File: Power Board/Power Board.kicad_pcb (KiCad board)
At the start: 2 copper layers, 55.9 x 58.4 mm, 55 parts, among them J1 Conn_02x10_Odd_Even, J2 Conn_01x02, J3 Conn_01x02, J4 Conn_01x02, J5 Conn_01x02, Q1 SI7135DP, Q2 SI7135DP, Q3 SI7135DP, Q4 SI7135DP, Q5 SI7135DP, Q6 SI7135DP, U1 LTC4417CGN, U2 TPS54308DDC, U3 LTC3130-1

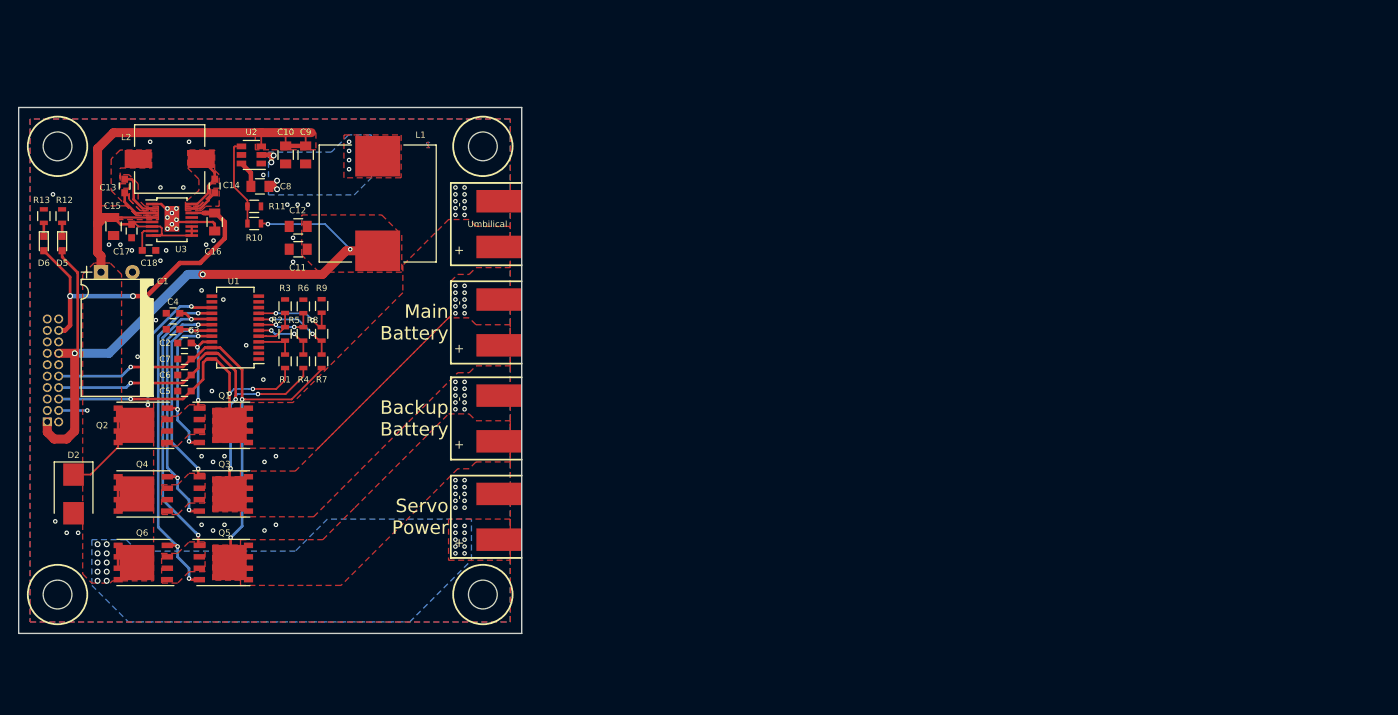
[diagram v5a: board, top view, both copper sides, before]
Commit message: Finally ready to redo power PCB
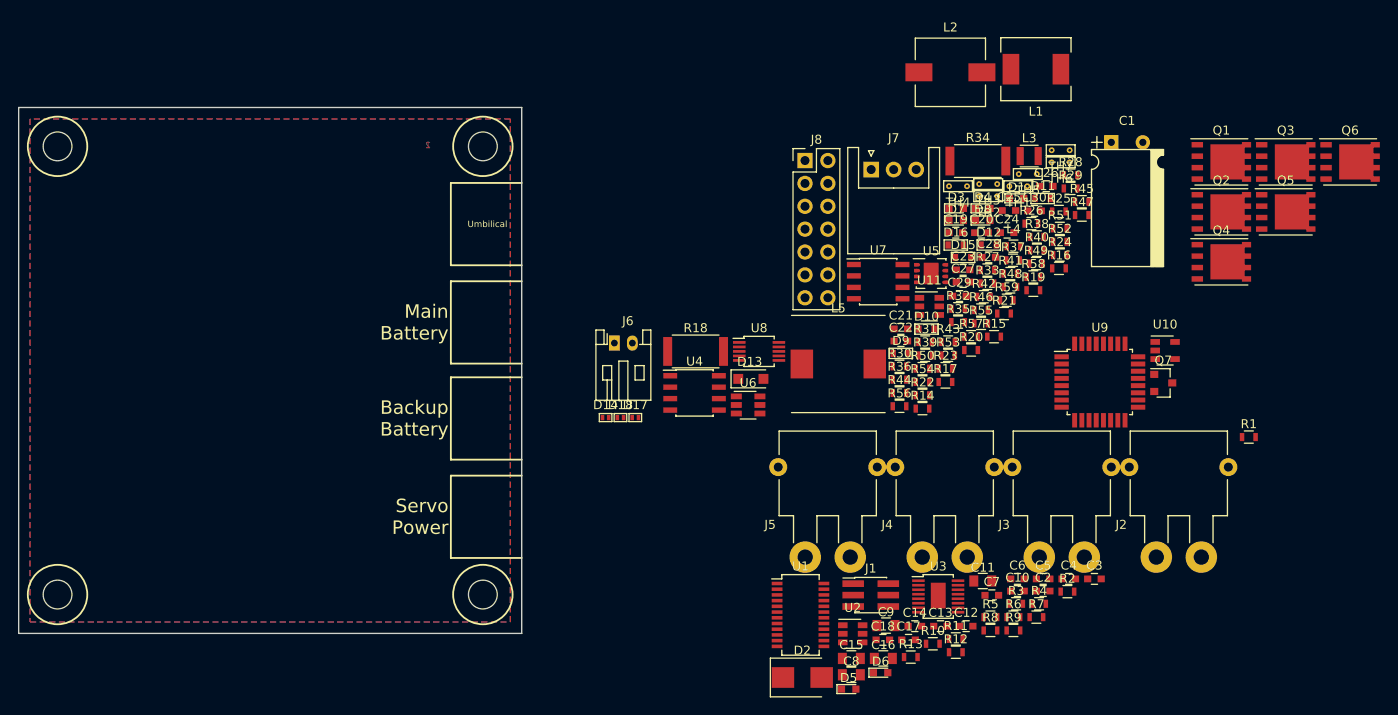
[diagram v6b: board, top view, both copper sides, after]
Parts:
- added C19: 0.1 µF, Capacitors_SMD:C_0603, F.Cu at (299.9, 97.0)
- added C20: 0.1 µF, Capacitors_SMD:C_0603, F.Cu at (302.8, 97.0)
- added C21: 0.1 µF, Capacitors_SMD:C_0603, F.Cu at (293.8, 107.7)
- added C22: 0.1 µF, Capacitors_SMD:C_0603, F.Cu at (293.8, 109.0)
- added C23: 0.33 µF, Capacitors_SMD:C_0603, F.Cu at (300.7, 101.1)
- added C24: 10 µF, Capacitors_SMD:C_0603, F.Cu at (305.6, 97.0)
- added C25: 10 µF, Capacitors_SMD:C_0603, F.Cu at (305.8, 94.5)
- added C26: 0.1 µF, Capacitors_SMD:C_0603, F.Cu at (310.0, 91.8)
- added C27: 0.1 µF, Capacitors_SMD:C_0603, F.Cu at (300.7, 102.4)
- added C28: 4.7 µF, Capacitors_SMD:C_0603, F.Cu at (303.6, 99.7)
- added C29: 270 pF, Capacitors_SMD:C_0603, F.Cu at (300.3, 104.0)
- added C30: 10 µF, Capacitors_SMD:C_0603, F.Cu at (308.7, 94.5)
- added D1: LED_B, LEDs:LED_0603, F.Cu at (306.7, 93.2)
- added D10: 12V TVS, Custom Parts:TVS_0603, F.Cu at (296.7, 107.7)
- added D11: 12V TVS, Custom Parts:TVS_0603, F.Cu at (309.6, 93.2)
- added D12: 12V TVS, Custom Parts:TVS_0603, F.Cu at (303.6, 98.3)
- added D13: D_Schottky, Diodes_SMD:D_SOD-123F, F.Cu at (277.2, 113.2)
- added D14: 3.3V TVS, Custom Parts:TVS_0402, F.Cu at (261.0, 117.5)
- added D15: 12V TVS, Custom Parts:TVS_0603, F.Cu at (300.7, 99.7)
- added D16: 12V TVS, Custom Parts:TVS_0603, F.Cu at (299.9, 98.3)
- added D17: 3.3V TVS, Custom Parts:TVS_0402, F.Cu at (264.3, 117.5)
- added D18: 3.3V TVS, Custom Parts:TVS_0402, F.Cu at (262.7, 117.5)
- added D3: LED_B, LEDs:LED_0603, F.Cu at (300.0, 94.3)
- added D4: LED_B, LEDs:LED_0603, F.Cu at (302.9, 94.3)
- added D7: LED_B, LEDs:LED_0603, F.Cu at (300.0, 95.6)
- added D8: LED_G, LEDs:LED_0603, F.Cu at (302.9, 95.6)
- added D9: 12V TVS, Custom Parts:TVS_0603, F.Cu at (293.8, 110.4)
- added HS1: Heatsink, Custom Parts:HS_ATS1099, F.Cu at (270.8, 97.7)
- added J6: Conn_01x02, Connectors_JST:JST_PH_S2B-PH-K_02x2.00mm_Angled, F.Cu at (262.0, 109.2)
- added J7: Conn_01x03, Connectors_JST:JST_XH_S03B-XH-A_03x2.50mm_Angled, F.Cu at (290.5, 90.0)
- added J8: Conn_02x07_Odd_Even, Pin_Headers:Pin_Header_Straight_2x07_Pitch2.54mm, F.Cu at (283.2, 89.0)
- added L3: 10 µH, Custom Parts:L_1008, F.Cu at (308.1, 88.5)
- added L4: 220 Ω @ 100 MHz, Inductors_SMD:L_0603, F.Cu at (306.3, 98.5)
- added L5: 10 µH, Custom Parts:L_SLF10165, F.Cu at (286.9, 111.6)
- added Q7: DMG2305UX, TO_SOT_Packages_SMD:SOT-23, F.Cu at (323.0, 113.7)
- added R14: 1 kΩ, Resistors_SMD:R_0603, F.Cu at (296.2, 116.5)
- added R15: 1 kΩ, Resistors_SMD:R_0603, F.Cu at (304.2, 108.5)
- added R16: 1 kΩ, Resistors_SMD:R_0603, F.Cu at (311.4, 100.9)
- added R17: 1 kΩ, Resistors_SMD:R_0603, F.Cu at (298.8, 113.5)
- added R18: 0.124Ω, Resistors_SMD:R_2512, F.Cu at (271.0, 110.2)
- added R19: 8.25 kΩ, Resistors_SMD:R_0603, F.Cu at (308.5, 103.4)
- added R20: 1 kΩ, Resistors_SMD:R_0603, F.Cu at (301.6, 110.0)
- added R21: 22.1 kΩ, Resistors_SMD:R_0603, F.Cu at (305.3, 105.9)
- added R22: 100 Ω, Resistors_SMD:R_0603, F.Cu at (296.2, 115.0)
- added R23: 100 kΩ, Resistors_SMD:R_0603, F.Cu at (298.8, 112.1)
- added R24: 100 kΩ, Resistors_SMD:R_0603, F.Cu at (311.5, 99.4)
- added R25: 100 kΩ, Resistors_SMD:R_0603, F.Cu at (311.4, 94.6)
- added R26: 140 kΩ, Resistors_SMD:R_0603, F.Cu at (308.3, 96.0)
- added R27: 10 Ω, Resistors_SMD:R_0603, F.Cu at (303.4, 101.1)
- added R28: 10 kΩ, Resistors_SMD:R_0603, F.Cu at (312.7, 90.6)
- added R29: 10 kΩ, Resistors_SMD:R_0603, F.Cu at (312.7, 92.0)
- added R30: 100 kΩ, Resistors_SMD:R_0603, F.Cu at (293.7, 111.8)
- added R31: 100 kΩ, Resistors_SMD:R_0603, F.Cu at (296.5, 109.1)
- added R32: 100 kΩ, Resistors_SMD:R_0603, F.Cu at (300.2, 105.4)
- added R33: 10 kΩ, Resistors_SMD:R_0603, F.Cu at (303.4, 102.6)
- added R34: 2.5 mΩ, Resistors_SMD:R_2512, F.Cu at (302.4, 89.0)
- added R35: 10 kΩ, Resistors_SMD:R_0603, F.Cu at (300.2, 106.9)
- added R36: 10 kΩ, Resistors_SMD:R_0603, F.Cu at (293.7, 113.3)
- added R37: 64.9 kΩ, Resistors_SMD:R_0603, F.Cu at (306.3, 100.0)
- added R38: 64.9 kΩ, Resistors_SMD:R_0603, F.Cu at (308.9, 97.4)
- added R39: 121 kΩ, Resistors_SMD:R_0603, F.Cu at (296.5, 110.6)
- added R40: 121 kΩ, Resistors_SMD:R_0603, F.Cu at (308.9, 98.9)
- added R41: 121 kΩ, Resistors_SMD:R_0603, F.Cu at (306.0, 101.5)
- added R42: 10 kΩ, Resistors_SMD:R_0603, F.Cu at (303.0, 104.1)
- added R43: 10 kΩ, Resistors_SMD:R_0603, F.Cu at (299.1, 109.1)
- added R44: 10 kΩ, Resistors_SMD:R_0603, F.Cu at (293.7, 114.8)
- added R45: 64.9 kΩ, Resistors_SMD:R_0603, F.Cu at (313.9, 93.5)
- added R46: 64.9 kΩ, Resistors_SMD:R_0603, F.Cu at (302.7, 105.6)
- added R47: 121 kΩ, Resistors_SMD:R_0603, F.Cu at (313.9, 95.0)
- added R48: 121 kΩ, Resistors_SMD:R_0603, F.Cu at (306.0, 103.0)
- added R49: 121 kΩ, Resistors_SMD:R_0603, F.Cu at (308.8, 100.4)
- added R50: 10 kΩ, Resistors_SMD:R_0603, F.Cu at (296.2, 112.1)
- added R51: 10 kΩ, Resistors_SMD:R_0603, F.Cu at (311.5, 96.5)
- added R52: 10 kΩ, Resistors_SMD:R_0603, F.Cu at (311.5, 98.0)
- added R53: 121 kΩ, Resistors_SMD:R_0603, F.Cu at (299.1, 110.6)
- added R54: 64.9 kΩ, Resistors_SMD:R_0603, F.Cu at (296.2, 113.5)
- added R55: 64.9 kΩ, Resistors_SMD:R_0603, F.Cu at (302.7, 107.0)
- added R56: 10 kΩ, Resistors_SMD:R_0603, F.Cu at (293.7, 116.2)
- added R57: 95.3 kΩ, Resistors_SMD:R_0603, F.Cu at (301.6, 108.5)
- added R58: 51 kΩ, Resistors_SMD:R_0603, F.Cu at (308.5, 101.9)
- added R59: 13.3 kΩ, Resistors_SMD:R_0603, F.Cu at (305.6, 104.5)
- added TH1: NXFT15XH103FA2B100, Custom Parts:Thermistor_Through_Hole_Tiny, F.Cu at (306.9, 91.8)
- added TH2: NXFT15XH103FA2B100, Custom Parts:Thermistor_Through_Hole_Tiny, F.Cu at (303.5, 92.9)
- added TH3: NXFT15XH103FA2B100, Custom Parts:Thermistor_Through_Hole_Tiny, F.Cu at (303.5, 91.6)
- added TH4: NXFT15XH103FA2B100, Custom Parts:Thermistor_Through_Hole_Tiny, F.Cu at (300.2, 91.8)
- added TH5: NXFT15XH103FA2B100, Custom Parts:Thermistor_Through_Hole_Tiny, F.Cu at (307.9, 90.5)
- added TH6: NXFT15XH103FA2B100, Custom Parts:Thermistor_Through_Hole_Tiny, F.Cu at (311.6, 89.2)
- added TH7: NXFT15XH103FA2B100, Custom Parts:Thermistor_Through_Hole_Tiny, F.Cu at (311.6, 87.8)
- added U10: LMR62014XMF, TO_SOT_Packages_SMD:SOT-23-5, F.Cu at (323.2, 110.1)
- added U11: TPS22810, TO_SOT_Packages_SMD:SOT-23-6, F.Cu at (297.0, 105.2)
- added U4: BQ2057WSNTR, Housings_SOIC:SOIC-8_3.9x4.9mm_Pitch1.27mm, F.Cu at (270.9, 114.8)
- added U5: BQ29209DRBT, Housings_SON:Texas_S-PVSON-N8, F.Cu at (297.2, 101.5)
- added U6: LT6700CS6-1, TO_SOT_Packages_SMD:TSOT-23-6, F.Cu at (276.9, 116.1)
- added U7: STS8C5H30L, Housings_SOIC:SOIC-8_3.9x4.9mm_Pitch1.27mm, F.Cu at (291.3, 102.4)
- added U8: LTC4150, Housings_SSOP:MSOP-10_3x3mm_Pitch0.5mm, F.Cu at (278.1, 110.2)
- added U9: ATxmega32E5-AU, Housings_QFP:TQFP-32_7x7mm_Pitch0.8mm, F.Cu at (315.9, 113.6)
- C1: value 470 uF -> 470 µF; footprint Custom Footprints:CP_Radial_Horiz_D8.0mm_L13.00mm_P3.50mm -> Custom Parts:CP_Radial_Horiz_D8.0mm_L13.00mm_P3.50mm
- C10: value 15 uF -> 4.7 µF; footprint Capacitors_SMD:C_0805 -> Capacitors_SMD:C_0603
- C11: value 22 uF -> 47 µF
- C12: value 22 uF -> 4.7 µF; footprint Capacitors_SMD:C_0805 -> Capacitors_SMD:C_0603
- C15: value 15 uF -> 15 µF
- C16: value 22 uF -> 22 µF
- C17: value 1 uF -> 1 µF
- C18: value 4.7 uF -> 4.7 µF
- C2, C3, C4, C5, C6, C7, C8: value 0.1 uF -> 0.1 µF
- C9: value 15 uF -> 22 µF
- J1: value Conn_02x10_Odd_Even -> Conn_02x03_Odd_Even; footprint Pin_Headers:Pin_Header_Straight_2x10_Pitch1.27mm -> Pin_Headers:Pin_Header_Straight_2x03_Pitch1.27mm_SMD; moved to F.Cu
- J2, J3, J4, J5: footprint Custom Footprints:High_Current_Wires -> Custom Parts:XT30_Angled
- L1: value 18 uH -> 2.2 µH; footprint Inductors_SMD:L_Wuerth_HCI-1365 -> Custom Parts:L_SRP6540
- L2: value 15 uH -> 15 µH; footprint Custom Footprints:L_Wuerth_7447779115 -> Custom Parts:L_Wuerth_7447779115
- Q1, Q2, Q3, Q4, Q5, Q6: value SI7135DP -> SI7157DP; footprint Custom Footprints:PowerPAK_SO-8 -> Custom Parts:PowerPAK_SO-8
- R10: value 100 kΩ -> 33.2 kΩ
- R11: value 22 kΩ -> 10 kΩ
- U2: value TPS54308DDC -> TPS564208DDCT
- moved Q6 141.2 mm to (343.7, 89.1), turned to 0 degrees
- moved Q5 124.3 mm to (336.6, 94.7)
- moved Q3 123.6 mm to (336.6, 89.1)
- moved Q4 122.5 mm to (329.4, 100.2), turned to 0 degrees
- moved Q2 122.1 mm to (329.4, 94.7), turned to 0 degrees
- moved Q1 114.7 mm to (329.4, 89.1)
- moved C1 113.1 mm to (317.2, 86.9)
- moved R12 110.5 mm to (299.9, 143.6), turned to 0 degrees
- moved R13 108.0 mm to (294.9, 144.1), turned to 0 degrees
- moved R1 107.4 mm to (332.5, 119.7), turned to 0 degrees
- moved C3 106.0 mm to (315.3, 135.4), turned to 0 degrees
- moved D6 104.5 mm to (291.6, 145.8), turned to 0 degrees
- moved C4 103.8 mm to (312.5, 135.4), turned to 0 degrees
- moved C13 103.0 mm to (298.2, 140.7), turned to 0 degrees
- moved D5 100.4 mm to (288.0, 147.7), turned to 0 degrees
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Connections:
- C10 pad 1: /VCC_IN -> GND
- C10 pad 2: GND -> /BAT_CELL_2
- C12 pad 1: +3V3 -> Net-(C12-Pad1)
- C12 pad 2: GND -> Net-(C12-Pad2)
- C6 pad 2: /BAT_VCC -> /BAT_CELL_2
- J1 pad 1: +3V3 -> Net-(J1-Pad1)
- J1 pad 2: GND -> +3V3
- J1 pad 4: /VCC_IN -> (no net)
- J1 pad 5: (no net) -> Net-(J1-Pad5)
- J1 pad 6: /UMB_VCC -> GND
- J4 pad 1: /BAT_VCC -> /BAT_CELL_2_CONN
- Q3 pad 1: /BAT_VCC -> /BAT_CELL_2
- R4 pad 2: /BAT_VCC -> /BAT_CELL_2
- U1 pad 10: (no net) -> /SEL_~VALID1~
- U1 pad 11: (no net) -> /SEL_~VALID2~
- U1 pad 12: (no net) -> /SEL_~VALID3~
- U1 pad 2: (no net) -> /SEL_~SHDN~
- U1 pad 23: /BAT_VCC -> /BAT_CELL_2
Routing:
- net /VCC_IN: track 106.1 -> 0.00 mm, vias 23 -> 0
- net +3V3: track 80.1 -> 0.00 mm, vias 4 -> 0
- net /BAT_BAK_VCC: track 56.9 -> 0.00 mm, vias 3 -> 0
- net /BAT_VCC: track 46.2 -> 0.00 mm, vias 4 -> 0
- net /UMB_VCC: track 45.5 -> 0.00 mm, vias 3 -> 0
- net +12V: track 37.9 -> 0.00 mm, vias 2 -> 0
- net Net-(Q5-Pad2): track 37.7 -> 0.00 mm, vias 3 -> 0
- net Net-(C4-Pad1): track 32.6 -> 0.00 mm, vias 2 -> 0
- net Net-(Q3-Pad2): track 27.9 -> 0.00 mm, vias 3 -> 0
- net Net-(C3-Pad1): track 22.6 -> 0.00 mm, vias 2 -> 0
- net Net-(Q1-Pad2): track 18.0 -> 0.00 mm, vias 3 -> 0
- net Net-(R10-Pad2): track 10.2 -> 0.00 mm
- net Net-(C2-Pad1): track 9.60 -> 0.00 mm, vias 2 -> 0
- net Net-(R7-Pad1): track 9.53 -> 0.00 mm, vias 2 -> 0
- net Net-(R8-Pad2): track 9.28 -> 0.00 mm, vias 2 -> 0
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- removed copper zone on F.Cu, net +3V3
- removed copper zone on F.Cu, net /BAT_BAK_VCC
- removed copper zone on F.Cu, net /BAT_VCC
- removed copper zone on F.Cu, net /UMB_VCC
- removed copper zone on B.Cu, net /VCC_IN
- removed copper zone on F.Cu, net /VCC_IN
- removed copper zone on F.Cu, net Net-(C13-Pad1)
- removed copper zone on F.Cu, net Net-(C13-Pad2)
- removed copper zone on F.Cu, net Net-(C14-Pad1)
- removed copper zone on F.Cu, net Net-(C14-Pad2)
- removed copper zone on F.Cu, net Net-(C2-Pad1)
- removed copper zone on F.Cu, net Net-(C3-Pad1)
- removed copper zone on F.Cu, net Net-(C4-Pad1)
- removed copper zone on B.Cu, net Net-(C8-Pad2)
- removed copper zone on F.Cu, net Net-(C8-Pad2)

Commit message: Switching to a screw terminal for power board
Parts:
- moved J8 84.9 mm to (199.7, 104.6)
- moved J2 76.5 mm to (256.4, 167.5), turned to 270 degrees
- moved J3 59.3 mm to (256.4, 154.5), turned to 270 degrees
- moved J4 43.1 mm to (256.4, 141.5), turned to 270 degrees
- moved U9 41.9 mm to (356.9, 104.9)
- moved J5 29.6 mm to (256.4, 128.5), turned to 270 degrees
- moved J6 25.3 mm to (279.7, 91.1)
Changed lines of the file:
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@@
   )
   (module Connectors_JST:JST_PH_S2B-PH-K_02x2.00mm_Angled (layer F.Cu)
-    (at 262.004 109.228)
+    (at 279.704 91.128)
     (descr "JST PH series connector, S2B-PH-K, side entry type, through hole, Datasheet: http://www.jst-mfg.com/product/pdf/eng/ePH.pdf")
     (tags "connector jst ph")
@@
   )
   (module Pin_Headers:Pin_Header_Straight_2x07_Pitch2.54mm (layer F.Cu)
-    (at 283.179001 88.953001)
+    (at 199.704 104.648)
     (descr "Through hole straight pin header, 2x07, 2.54mm pitch, double rows")
     (tags "Through hole pin header THT 2x07 2.54mm double row")
@@
   )
   (module Housings_QFP:TQFP-32_7x7mm_Pitch0.8mm (layer F.Cu)
-    (at 315.929001 113.553001)
+    (at 356.904 104.928)
     (descr "32-Lead Plastic Thin Quad Flatpack (PT) - 7x7x1.0 mm Body, 2.00 mm [TQFP] (see Microchip Packaging Specification 00000049BS.pdf)")
     (tags "QFP 0.8")
@@
   )
   (module "Custom Parts:XT30_Angled" (layer F.Cu)
-    (at 324.704 133.003001)
-    (fp_text reference J2 (at -6.4 -3.6) (layer F.SilkS)
+    (at 256.428999 167.528 270)
+    (fp_text reference J2 (at -6.4 -3.6 270) (layer F.SilkS)
       (effects (font (size 1 1) (thickness 0.15)))
     )
-    (fp_text value Conn_01x02 (at 0 2.6) (layer F.Fab)
+    (fp_text value Conn_01x02 (at 0 2.6 270) (layer F.Fab)
       (effects (font (size 1 1) (thickness 0.15)))
     )
@@
     (fp_line (start 1.6 0) (end 1.6 -5) (layer F.Fab) (width 0.15))
     (fp_line (start 3.4 0) (end 3.4 -5) (layer F.Fab) (width 0.15))
-    (pad "" thru_hole circle (at 5.5 -10) (size 2 2) (drill 1) (layers *.Cu *.Mask))
-    (pad "" thru_hole circle (at -5.5 -10) (size 2 2) (drill 1) (layers *.Cu *.Mask))
-    (pad 2 thru_hole circle (at 2.5 0) (size 3.5 3.5) (drill 1.7) (layers *.Cu *.Mask)
+    (pad "" thru_hole circle (at 5.5 -10 270) (size 2 2) (drill 1) (layers *.Cu *.Mask))
+    (pad "" thru_hole circle (at -5.5 -10 270) (size 2 2) (drill 1) (layers *.Cu *.Mask))
+    (pad 2 thru_hole circle (at 2.5 0 270) (size 3.5 3.5) (drill 1.7) (layers *.Cu *.Mask)
       (net 2 GND))
-    (pad 1 thru_hole circle (at -2.5 0) (size 3.5 3.5) (drill 1.7) (layers *.Cu *.Mask)
+    (pad 1 thru_hole circle (at -2.5 0 270) (size 3.5 3.5) (drill 1.7) (layers *.Cu *.Mask)
       (net 21 /VCC_IN))
   )
   (module "Custom Parts:XT30_Angled" (layer F.Cu)
-    (at 311.704 133.003001)
-    (fp_text reference J3 (at -6.4 -3.6) (layer F.SilkS)
+    (at 256.428999 154.528 270)
+    (fp_text reference J3 (at -6.4 -3.6 270) (layer F.SilkS)
       (effects (font (size 1 1) (thickness 0.15)))
     )
-    (fp_text value Conn_01x02 (at 0 2.6) (layer F.Fab)
+    (fp_text value Conn_01x02 (at 0 2.6 270) (layer F.Fab)
       (effects (font (size 1 1) (thickness 0.15)))
     )
@@
     (fp_line (start 1.2 -4.6) (end 1.2 -1.6) (layer F.SilkS) (width 0.15))
     (fp_line (start 3.8 -1.6) (end 3.8 -4.6) (layer F.SilkS) (width 0.15))
-    (pad 1 thru_hole circle (at -2.5 0) (size 3.5 3.5) (drill 1.7) (layers *.Cu *.Mask)
+    (pad 1 thru_hole circle (at -2.5 0 270) (size 3.5 3.5) (drill 1.7) (layers *.Cu *.Mask)
       (net 7 /BAT_BAK_VCC))
-    (pad 2 thru_hole circle (at 2.5 0) (size 3.5 3.5) (drill 1.7) (layers *.Cu *.Mask)
+    (pad 2 thru_hole circle (at 2.5 0 270) (size 3.5 3.5) (drill 1.7) (layers *.Cu *.Mask)
       (net 2 GND))
-    (pad "" thru_hole circle (at -5.5 -10) (size 2 2) (drill 1) (layers *.Cu *.Mask))
-    (pad "" thru_hole circle (at 5.5 -10) (size 2 2) (drill 1) (layers *.Cu *.Mask))
+    (pad "" thru_hole circle (at -5.5 -10 270) (size 2 2) (drill 1) (layers *.Cu *.Mask))
+    (pad "" thru_hole circle (at 5.5 -10 270) (size 2 2) (drill 1) (layers *.Cu *.Mask))
   )
   (module "Custom Parts:XT30_Angled" (layer F.Cu)
-    (at 298.704 133.003001)
-    (fp_text reference J4 (at -6.4 -3.6) (layer F.SilkS)
+    (at 256.428999 141.528 270)
+    (fp_text reference J4 (at -6.4 -3.6 270) (layer F.SilkS)
       (effects (font (size 1 1) (thickness 0.15)))
     )
-    (fp_text value Conn_01x02 (at 0 2.6) (layer F.Fab)
+    (fp_text value Conn_01x02 (at 0 2.6 270) (layer F.Fab)
       (effects (font (size 1 1) (thickness 0.15)))
     )
@@
     (fp_line (start 1.6 0) (end 1.6 -5) (layer F.Fab) (width 0.15))
     (fp_line (start 3.4 0) (end 3.4 -5) (layer F.Fab) (width 0.15))
-    (pad "" thru_hole circle (at 5.5 -10) (size 2 2) (drill 1) (layers *.Cu *.Mask))
-    (pad "" thru_hole circle (at -5.5 -10) (size 2 2) (drill 1) (layers *.Cu *.Mask))
-    (pad 2 thru_hole circle (at 2.5 0) (size 3.5 3.5) (drill 1.7) (layers *.Cu *.Mask)
+    (pad "" thru_hole circle (at 5.5 -10 270) (size 2 2) (drill 1) (layers *.Cu *.Mask))
+    (pad "" thru_hole circle (at -5.5 -10 270) (size 2 2) (drill 1) (layers *.Cu *.Mask))
+    (pad 2 thru_hole circle (at 2.5 0 270) (size 3.5 3.5) (drill 1.7) (layers *.Cu *.Mask)
       (net 2 GND))
-    (pad 1 thru_hole circle (at -2.5 0) (size 3.5 3.5) (drill 1.7) (layers *.Cu *.Mask)
+    (pad 1 thru_hole circle (at -2.5 0 270) (size 3.5 3.5) (drill 1.7) (layers *.Cu *.Mask)
       (net 47 /BAT_CELL_2_CONN))
   )
   (module "Custom Parts:XT30_Angled" (layer F.Cu)
-    (at 285.704 133.003001)
-    (fp_text reference J5 (at -6.4 -3.6) (layer F.SilkS)
+    (at 256.428999 128.528 270)
+    (fp_text reference J5 (at -6.4 -3.6 270) (layer F.SilkS)
       (effects (font (size 1 1) (thickness 0.15)))
     )
-    (fp_text value Conn_01x02 (at 0 2.6) (layer F.Fab)
+    (fp_text value Conn_01x02 (at 0 2.6 270) (layer F.Fab)
       (effects (font (size 1 1) (thickness 0.15)))
     )
@@
     (fp_line (start 1.2 -4.6) (end 1.2 -1.6) (layer F.SilkS) (width 0.15))
     (fp_line (start 3.8 -1.6) (end 3.8 -4.6) (layer F.SilkS) (width 0.15))
-    (pad 1 thru_hole circle (at -2.5 0) (size 3.5 3.5) (drill 1.7) (layers *.Cu *.Mask)
+    (pad 1 thru_hole circle (at -2.5 0 270) (size 3.5 3.5) (drill 1.7) (layers *.Cu *.Mask)
       (net 6 /UMB_VCC))
-    (pad 2 thru_hole circle (at 2.5 0) (size 3.5 3.5) (drill 1.7) (layers *.Cu *.Mask)
+    (pad 2 thru_hole circle (at 2.5 0 270) (size 3.5 3.5) (drill 1.7) (layers *.Cu *.Mask)
       (net 2 GND))
-    (pad "" thru_hole circle (at -5.5 -10) (size 2 2) (drill 1) (layers *.Cu *.Mask))
-    (pad "" thru_hole circle (at 5.5 -10) (size 2 2) (drill 1) (layers *.Cu *.Mask))
+    (pad "" thru_hole circle (at -5.5 -10 270) (size 2 2) (drill 1) (layers *.Cu *.Mask))
+    (pad "" thru_hole circle (at 5.5 -10 270) (size 2 2) (drill 1) (layers *.Cu *.Mask))
   )
   (module Resistors_SMD:R_0603 (layer F.Cu)
@@
     (connect_pads (clearance 0.25))
     (min_thickness 0.25)
-    (fill yes (arc_segments 32) (thermal_gap 0.25) (thermal_bridge_width 0.5))
+    (fill (arc_segments 32) (thermal_gap 0.25) (thermal_bridge_width 0.5))
     (polygon
       (pts
@@
     (connect_pads (clearance 0.25))
     (min_thickness 0.25)
-    (fill yes (arc_segments 32) (thermal_gap 0.25) (thermal_bridge_width 0.5))
+    (fill (arc_segments 32) (thermal_gap 0.25) (thermal_bridge_width 0.5))
     (polygon
       (pts
